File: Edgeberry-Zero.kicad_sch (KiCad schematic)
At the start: 28 parts, among them J1 Molex_KK_1x02_P2.54mm, J2 Raspberry_Pi_2_3, J3 Edgeberry Cartridge Connector, P1 12Vin, Q1 BC547, Q2 BC547, Q3 BC547, SW1 SW_PUSH, U1 24LC256, U2 LM2596S-5.0

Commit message: Finished design
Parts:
- added J4: Conn_01x04_Pin, Connector_PinHeader_2.54mm:PinHeader_1x04_P2.54mm_Horizontal, symbol Connector:Conn_01x04_Pin
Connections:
- net +3V3: now also J4.2 (Pin_2)
- net GND: now also J4.1 (Pin_1)
- net ID_SCL: now also J4.3 (Pin_3)
- net ID_SDA: now also J4.4 (Pin_4)

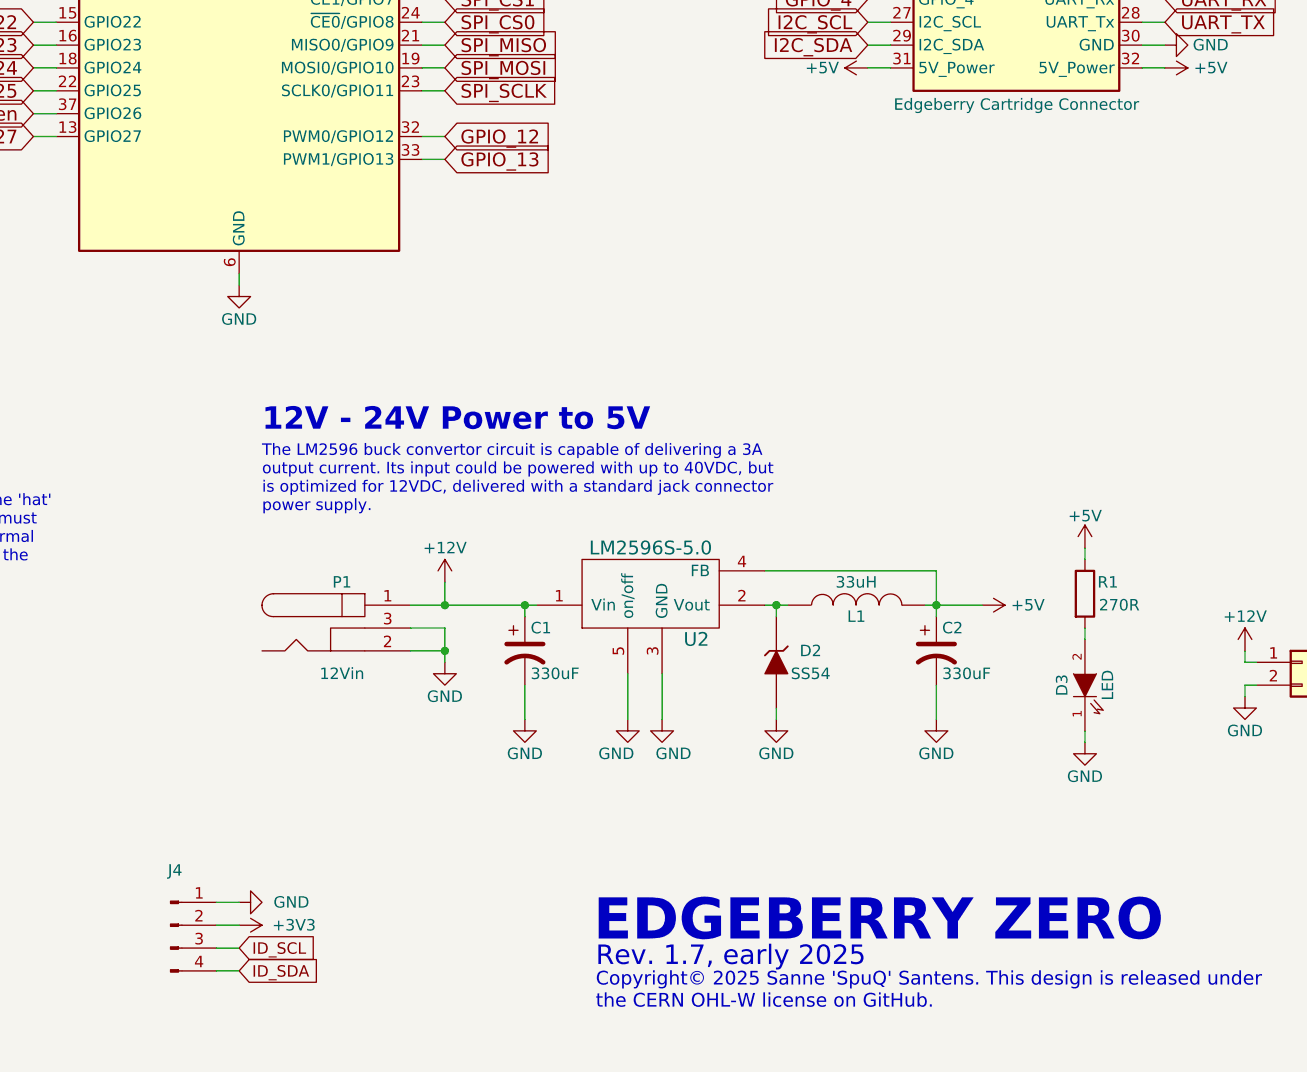
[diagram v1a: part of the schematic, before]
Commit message: Improvements: C2, J4 (ext)
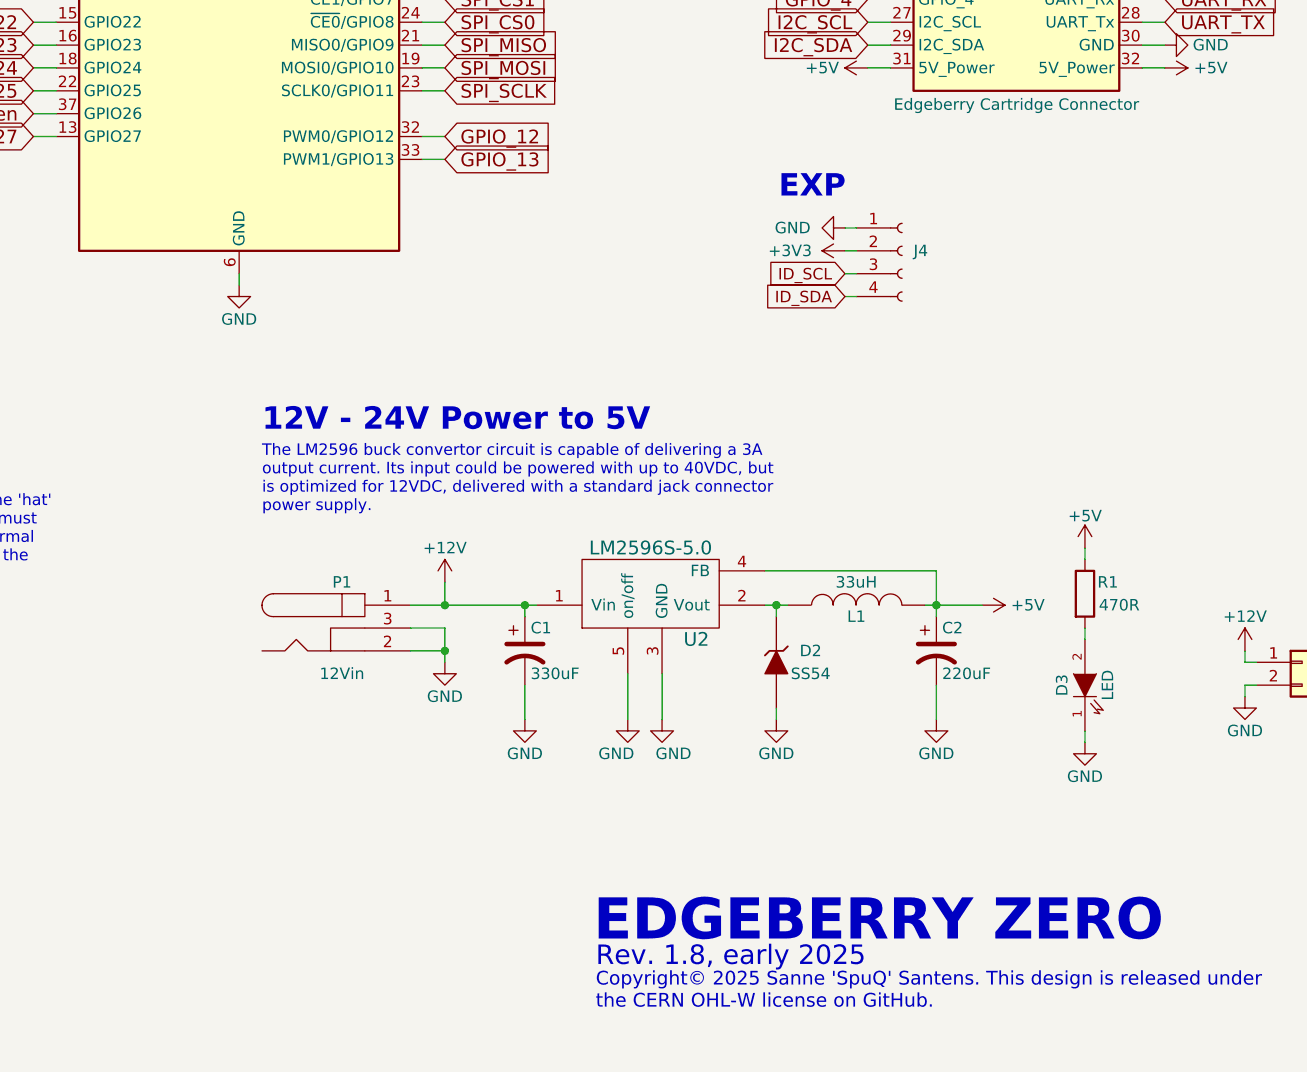
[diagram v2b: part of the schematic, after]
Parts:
- removed J4: Conn_01x04_Pin, Connector_PinHeader_2.54mm:PinHeader_1x04_P2.54mm_Horizontal, symbol Connector:Conn_01x04_Pin
- added J4: Conn_01x04_Socket, Connector_PinSocket_2.00mm:PinSocket_1x04_P2.00mm_Horizontal, symbol Connector:Conn_01x04_Socket
- C2: value 330uF -> 220uF
- R1: value 270R -> 470R
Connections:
- net +3V3: now also J4.2 (Pin_2)
- net GND: now also J4.1 (Pin_1)
- net ID_SCL: now also J4.3 (Pin_3)
- net ID_SDA: now also J4.4 (Pin_4)
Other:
- note added: "EXP"
- note added: "Rev. 1.8, early 2025"
- note removed: "Rev. 1.7, early 2025"

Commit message: Rev 1.8
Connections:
- net +3V3: now also J4.3 (Pin_3); no longer J4.2 (Pin_2)
- net GND: now also J4.4 (Pin_4); no longer J4.1 (Pin_1)
- net ID_SCL: now also J4.2 (Pin_2); no longer J4.3 (Pin_3)
- net ID_SDA: now also J4.1 (Pin_1); no longer J4.4 (Pin_4)
- net +12V renamed +Vin
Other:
- note added: "BASE BOARD Rev. 1.8, early 2025"
- note added: "Brings the Raspberry Pi Zero's I2C0 port to the edge of the board"
- note added: "Vin PWR"
- note removed: "Rev. 1.8, early 2025"
- moved on the sheet: J4
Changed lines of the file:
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@@
 		(title "Edgeberry Zero")
 		(date "2024-05-15")
-		(rev "1.7")
+		(rev "1.8")
 	)
 	(junction
@@
 	(wire
 		(pts
-			(xy 209.55 96.52) (xy 210.82 96.52)
+			(xy 260.35 107.95) (xy 261.62 107.95)
 		)
 		(stroke
@@
 	(wire
 		(pts
-			(xy 209.55 99.06) (xy 210.82 99.06)
+			(xy 260.35 110.49) (xy 261.62 110.49)
 		)
 		(stroke
@@
 	(wire
 		(pts
-			(xy 209.55 101.6) (xy 210.82 101.6)
+			(xy 260.35 113.03) (xy 261.62 113.03)
 		)
 		(stroke
@@
 	(wire
 		(pts
-			(xy 209.55 93.98) (xy 210.82 93.98)
+			(xy 260.35 105.41) (xy 261.62 105.41)
 		)
 		(stroke
@@
 		)
 	)
-	(text "Rev. 1.8, early 2025"
+	(text "BASE BOARD Rev. 1.8, early 2025"
 		(exclude_from_sim no)
 		(at 181.864 175.006 0)
@@
 		)
 	)
+	(text "Vin PWR"
+		(exclude_from_sim no)
+		(at 250.444 132.08 0)
+		(effects
+			(font
+				(size 2.4892 2.4892)
+				(thickness 0.4978)
+				(bold yes)
+			)
+			(justify left bottom)
+		)
+	)
+	(text "Brings the Raspberry Pi Zero's\nI2C0 port to the edge of the \nboard"
+		(exclude_from_sim no)
+		(at 248.158 101.092 0)
+		(effects
+			(font
+				(size 1.27 1.27)
+			)
+			(justify left bottom)
+		)
+	)
 	(text "RPi HAT ID EEPROM"
 		(exclude_from_sim no)
-		(at 20.32 116.84 0)
+		(at 20.32 120.65 0)
 		(effects
 			(font
@@
 	(text "EXP"
 		(exclude_from_sim no)
-		(at 202.184 90.932 0)
+		(at 247.396 94.234 0)
 		(effects
 			(font
@@
 	(global_label "ID_SDA"
 		(shape input)
-		(at 209.55 101.6 180)
+		(at 260.35 113.03 180)
 		(fields_autoplaced yes)
 		(effects
@@
 		)
 		(property "Intersheetrefs" "${INTERSHEET_REFS}"
-			(at 200.8085 101.6 0)
+			(at 251.6085 113.03 0)
 			(effects
 				(font
@@
 	(global_label "ID_SCL"
 		(shape input)
-		(at 209.55 99.06 180)
+		(at 260.35 110.49 180)
 		(fields_autoplaced yes)
 		(effects
@@
 		)
 		(property "Intersheetrefs" "${INTERSHEET_REFS}"
-			(at 200.869 99.06 0)
+			(at 251.669 110.49 0)
 			(effects
 				(font
@@
 			)
 		)
-		(property "Value" "+12V"
+		(property "Value" "+Vin"
 			(at 165.1 129.54 0)
 			(effects
@@
 			)
 		)
-		(property "Value" "+12V"
+		(property "Value" "+Vin"
 			(at 254 137.16 0)
 			(effects
@@
 	(symbol
 		(lib_id "EdgeBerry-rescue:+3V3")
-		(at 209.55 96.52 90)
+		(at 260.35 107.95 90)
 		(mirror x)
 		(unit 1)
@@
 		(dnp no)
 		(property "Reference" "#PWR23"
-			(at 213.36 96.52 0)
+			(at 264.16 107.95 0)
 			(effects
 				(font
@@
 		)
 		(property "Value" "+3V3"
-			(at 203.454 96.52 90)
+			(at 254.254 107.95 90)
 			(effects
 				(font
@@
 		)
 		(property "Footprint" ""
-			(at 209.55 96.52 0)
+			(at 260.35 107.95 0)
 			(effects
 				(font
@@
 		)
 		(property "Datasheet" ""
-			(at 209.55 96.52 0)
+			(at 260.35 107.95 0)
 			(effects
 				(font
@@
 		)
 		(property "Description" ""
-			(at 209.55 96.52 0)
+			(at 260.35 107.95 0)
 			(effects
 				(font
@@
 	(symbol
 		(lib_id "power:GND")
-		(at 209.55 93.98 270)
+		(at 260.35 105.41 270)
 		(mirror x)
 		(unit 1)
@@
 		(fields_autoplaced yes)
 		(property "Reference" "#PWR15"
-			(at 203.2 93.98 0)
+			(at 254 105.41 0)
 			(effects
 				(font
@@
 		)
 		(property "Value" "GND"
-			(at 205.74 93.9799 90)
+			(at 256.54 105.4099 90)
 			(effects
 				(font
@@
 		)
 		(property "Footprint" ""
-			(at 209.55 93.98 0)
+			(at 260.35 105.41 0)
 			(effects
 				(font
@@
 		)
 		(property "Datasheet" ""
-			(at 209.55 93.98 0)
+			(at 260.35 105.41 0)
 			(effects
 				(font
@@
 		)
 		(property "Description" ""
-			(at 209.55 93.98 0)
+			(at 260.35 105.41 0)
 			(effects
 				(font
@@
 		(dnp no)
 		(property "Reference" "J1"
-			(at 262.89 142.2399 0)
+			(at 262.89 143.51 0)
 			(effects
 				(font
@@
 	(symbol
 		(lib_id "Connector:Conn_01x04_Socket")
-		(at 215.9 96.52 0)
+		(at 266.7 110.49 0)
+		(mirror x)
 		(unit 1)
 		(exclude_from_sim no)
@@
 		(on_board yes)
 		(dnp no)
-		(fields_autoplaced yes)
 		(property "Reference" "J4"
-			(at 217.17 96.5199 0)
+			(at 267.716 108.966 0)
 			(effects
 				(font
@@
 		)
 		(property "Value" "Conn_01x04_Socket"
-			(at 217.17 99.0599 0)
+			(at 267.97 107.9501 0)
 			(effects
 				(font
@@
 		)
 		(property "Footprint" "Connector_PinSocket_2.00mm:PinSocket_1x04_P2.00mm_Horizontal"
-			(at 215.9 96.52 0)
+			(at 266.7 110.49 0)
 			(effects
 				(font
@@
 		)
 		(property "Datasheet" "~"
-			(at 215.9 96.52 0)
+			(at 266.7 110.49 0)
 			(effects
 				(font
@@
 		)
 		(property "Description" "Generic connector, single row, 01x04, script generated"
-			(at 215.9 96.52 0)
+			(at 266.7 110.49 0)
 			(effects
 				(font
